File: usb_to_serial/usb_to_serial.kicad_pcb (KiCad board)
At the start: 4 copper layers, 19 x 38.2 mm, 27 parts, among them J1 USB4105-GF-A, J2 RJ45_LED_Shielded, U1 FT232RL, U2 MAX3243CDBR

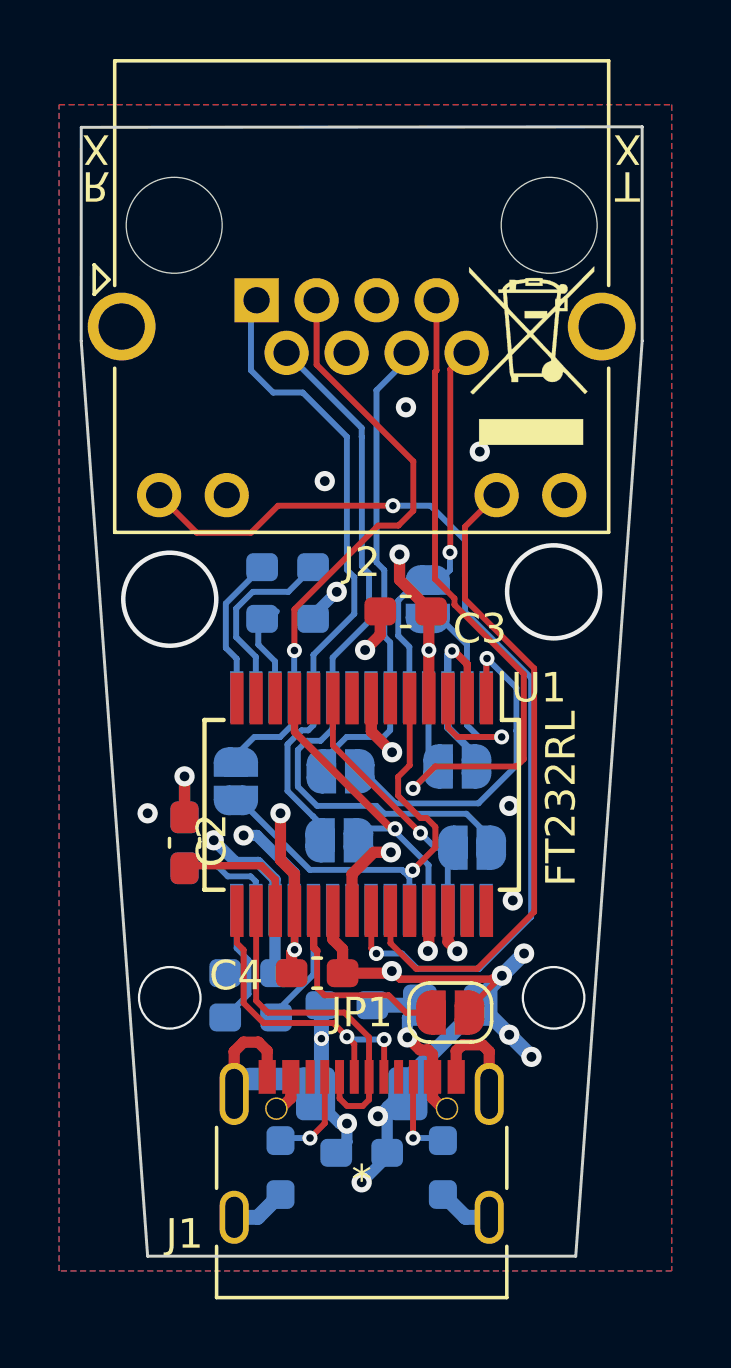
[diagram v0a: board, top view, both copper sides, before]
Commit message: Revision for Aisler design rules
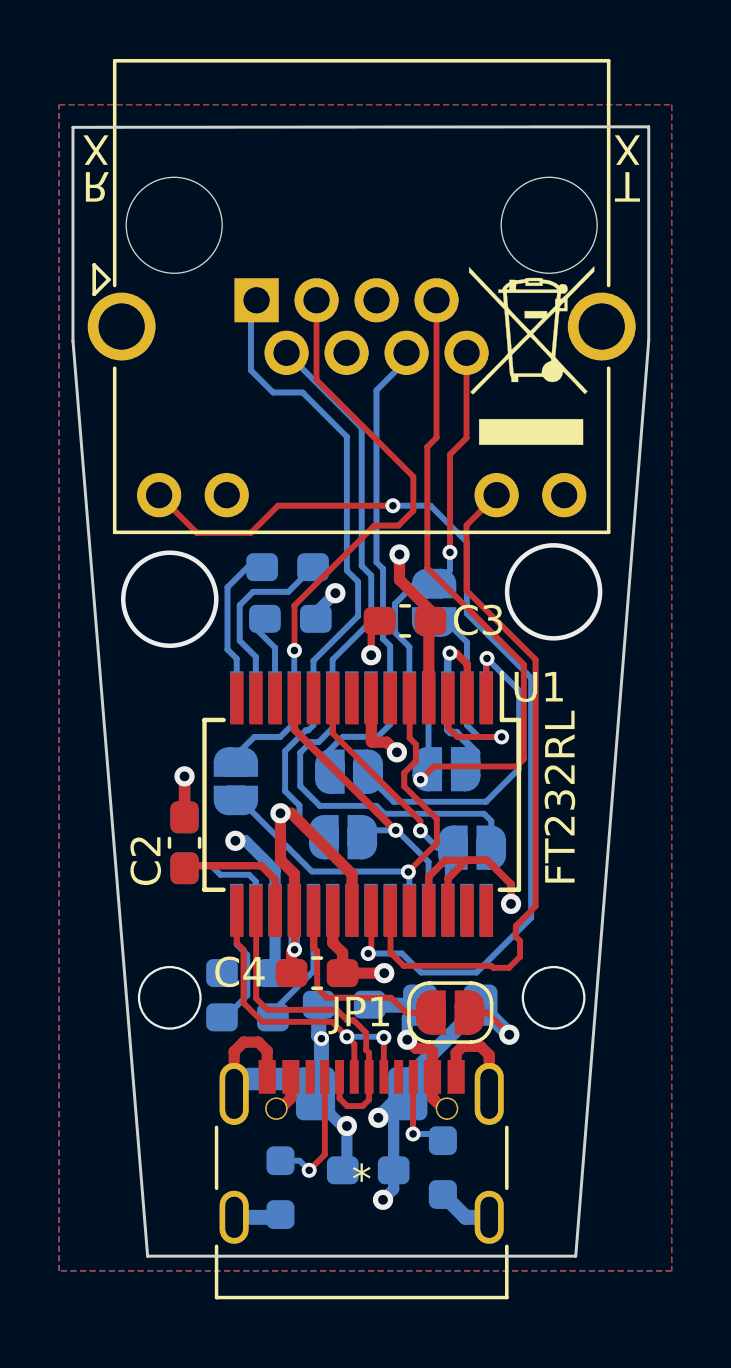
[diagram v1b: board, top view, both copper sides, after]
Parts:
- moved R1 0.68 mm to (133.0, 129.1)
- moved C8 0.63 mm to (136.0, 128.5)
- moved JP4 0.38 mm to (138.7, 114.9)
- moved C3 0.32 mm to (137.2, 109.9)
- moved JP2 0.29 mm to (135.3, 115.0)
- moved JP3 0.24 mm to (138.2, 109.3)
- moved JP6 0.17 mm to (135.2, 117.2)
- moved C10 0.11 mm to (131.9, 121.8)
- moved C7 0.11 mm to (131.9, 123.3)
- moved C9 0.09 mm to (133.4, 109.8)
- moved C6 0.09 mm to (135.2, 122.9)
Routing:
- net +5V: track 34.8 -> 27.3 mm, vias 10 -> 6
- net GND: track 46.2 -> 49.7 mm, vias 22 -> 13
- net Net-(J1-PadA5): track 3.31 -> 4.49 mm
- net TXLED#: track 22.6 -> 23.6 mm
- net DTR_EXT: track 24.6 -> 24.1 mm
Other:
- board size 19 x 38.2 mm -> 19.5 x 38.2 mm
- board text added: "Designed by Matt E Revised by vista 5/8/2024 REV3.5"
- board text removed: "Designed by Matt E 5/27/2022 REV2"

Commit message: Change USB-C connector footprint with one with NPTHs, add connections for forceon/forceoff on MAX3243
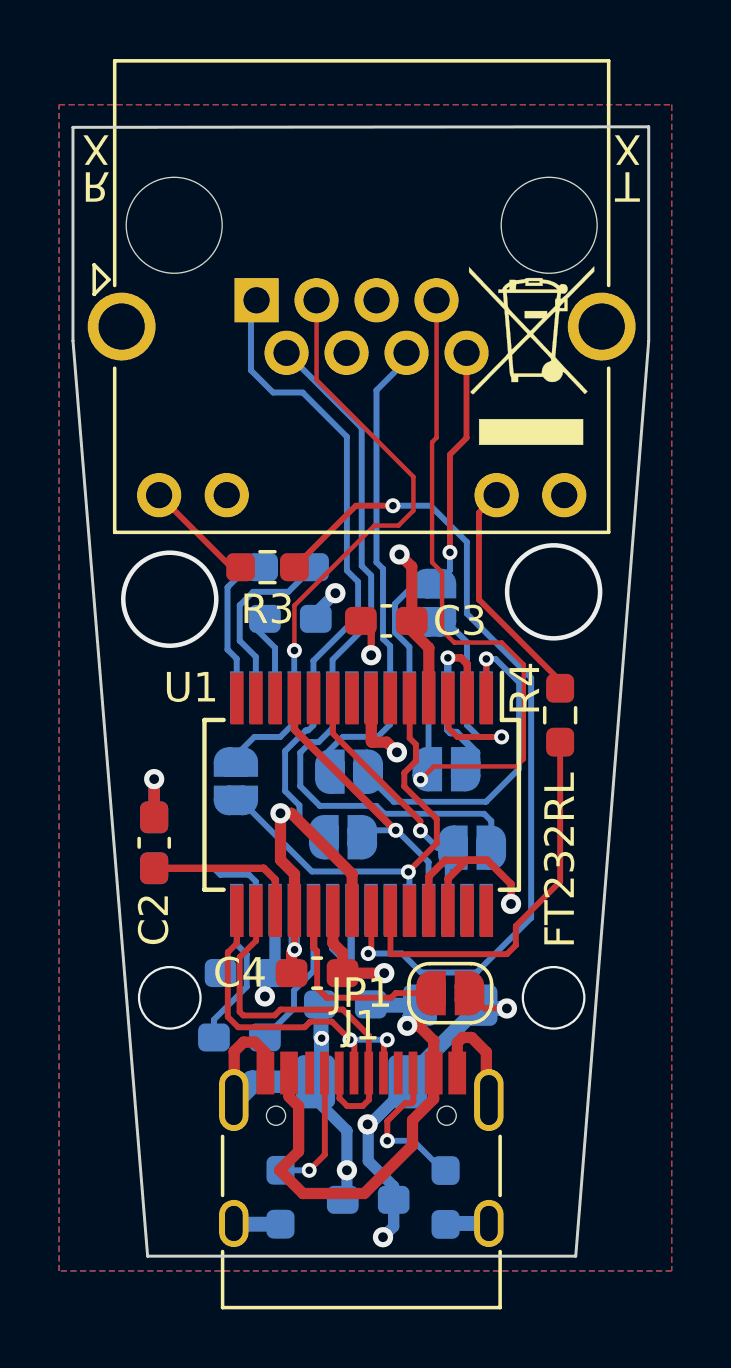
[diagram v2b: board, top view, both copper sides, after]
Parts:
- added R3: 330, Resistor_SMD:R_0603_1608Metric_Pad0.98x0.95mm_HandSolder, F.Cu at (132.6, 108.1)
- added R4: 330, Resistor_SMD:R_0603_1608Metric_Pad0.98x0.95mm_HandSolder, F.Cu at (142.5, 113.1)
- C11, C5, C9: value 100nF -> 330nF
- C7: value 100nF -> 47nF
- J1: value USB4105-GF-A -> USB4105; footprint Personal:USB4105-GF-A -> Connector_USB:USB_C_Receptacle_HRO_TYPE-C-31-M-12
- R1, R2: value 4.7K -> 5.1K
- moved C11 1.03 mm to (128.8, 117.4)
- moved C2 1.03 mm to (128.8, 117.4)
- moved R2 1.02 mm to (138.6, 129.4)
- moved C8 1.00 mm to (136.0, 129.5)
- moved C7 0.73 mm to (131.6, 124.0)
- moved JP1 0.66 mm to (138.8, 122.5)
- moved C3 0.64 mm to (136.6, 109.9)
- moved J1 0.43 mm to (135.8, 129.3)
- moved C1 0.41 mm to (135.8, 125.5)
- moved R1 0.32 mm to (133.0, 129.4)
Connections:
- J2 pad 11: TXLED# -> Net-(J2-Pad11)
- J2 pad 9: RXLED# -> Net-(J2-Pad9)
- U2 pad 22: unconnected-(U2-Pad22) -> +5V
- U2 pad 23: unconnected-(U2-Pad23) -> +5V
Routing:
- net TXLED#: track 23.6 -> 13.3 mm
- net Net-(J2-Pad11): track 0.00 -> 8.00 mm
- net RXLED#: track 33.5 -> 28.9 mm
- net Net-(J2-Pad9): track 0.00 -> 3.77 mm
- net VBUS: track 13.3 -> 16.8 mm
- net +5V: track 27.3 -> 30.6 mm
- net Net-(J1-CC2): track 3.04 -> 4.96 mm
- net USB_N: track 11.4 -> 12.6 mm
- net Net-(U2-C1+): track 4.11 -> 5.20 mm
- net USB_P: track 11.2 -> 12.2 mm
- net Net-(U2-V+): track 3.63 -> 4.58 mm
- net Net-(U1-3V3OUT): track 4.37 -> 5.33 mm
- net Net-(U2-C1-): track 4.17 -> 5.01 mm
- net DTR_EXT: track 24.1 -> 24.9 mm
- net GND: track 49.7 -> 50.3 mm
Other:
- board text added: "Designed by Matt E Revised by vista 5/9/2024 REV3.5"
- board text removed: "Designed by Matt E Revised by vista 5/8/2024 REV3.5"
